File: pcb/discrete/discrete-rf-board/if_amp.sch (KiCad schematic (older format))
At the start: 48 parts, among them Q23 NSVT65011MW6T1G, Q24 Q_NPN_BCE, Q25 NSVT65011MW6T1G, U10 NLAS4157DFT2G, U11 NLAS4157DFT2G, U8 NLAS4157DFT2G, U9 NLAS4157DFT2G

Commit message: Autofill
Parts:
- TP1, TP10, TP2, TP3, TP4, TP5, TP6, TP8, TP9: footprint (none) -> TestPoint:TestPoint_Pad_D1.0mm; Mouser (none) -> NoPart
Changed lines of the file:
@@
 F 0 "TP9" H 7300 2370 50  0000 C CNN
 F 1 "TestPoint" H 7300 2300 50  0000 C CNN
-F 2 "" H 7500 2100 50  0001 C CNN
+F 2 "TestPoint:TestPoint_Pad_D1.0mm" H 7500 2100 50  0001 C CNN
 F 3 "~" H 7500 2100 50  0001 C CNN
+F 4 "NoPart" H 7500 2100 50  0001 C CNN "Mouser"
 	1    7300 2100
 	1    0    0    -1
@@
 F 0 "TP8" H 6550 3620 50  0000 C CNN
 F 1 "TestPoint" H 6550 3550 50  0000 C CNN
-F 2 "" H 6750 3350 50  0001 C CNN
+F 2 "TestPoint:TestPoint_Pad_D1.0mm" H 6750 3350 50  0001 C CNN
 F 3 "~" H 6750 3350 50  0001 C CNN
+F 4 "NoPart" H 6750 3350 50  0001 C CNN "Mouser"
 	1    6550 3350
 	1    0    0    -1
@@
 F 0 "TP2" H 2050 3570 50  0000 C CNN
 F 1 "TestPoint" H 2050 3500 50  0000 C CNN
-F 2 "" H 2250 3300 50  0001 C CNN
+F 2 "TestPoint:TestPoint_Pad_D1.0mm" H 2250 3300 50  0001 C CNN
 F 3 "~" H 2250 3300 50  0001 C CNN
+F 4 "NoPart" H 2250 3300 50  0001 C CNN "Mouser"
 	1    2050 3300
 	-1   0    0    1
@@
 F 0 "TP1" H 1650 2670 50  0000 C CNN
 F 1 "TestPoint" H 1650 2600 50  0000 C CNN
-F 2 "" H 1850 2400 50  0001 C CNN
+F 2 "TestPoint:TestPoint_Pad_D1.0mm" H 1850 2400 50  0001 C CNN
 F 3 "~" H 1850 2400 50  0001 C CNN
+F 4 "NoPart" H 1850 2400 50  0001 C CNN "Mouser"
 	1    1650 2400
 	1    0    0    -1
@@
 F 0 "TP5" H 3250 2620 50  0000 C CNN
 F 1 "TestPoint" H 3250 2550 50  0000 C CNN
-F 2 "" H 3450 2350 50  0001 C CNN
+F 2 "TestPoint:TestPoint_Pad_D1.0mm" H 3450 2350 50  0001 C CNN
 F 3 "~" H 3450 2350 50  0001 C CNN
+F 4 "NoPart" H 3450 2350 50  0001 C CNN "Mouser"
 	1    3250 2350
 	1    0    0    -1
@@
 F 0 "TP4" H 2350 4220 50  0000 C CNN
 F 1 "TestPoint" H 2350 4150 50  0000 C CNN
-F 2 "" H 2550 3950 50  0001 C CNN
+F 2 "TestPoint:TestPoint_Pad_D1.0mm" H 2550 3950 50  0001 C CNN
 F 3 "~" H 2550 3950 50  0001 C CNN
+F 4 "NoPart" H 2550 3950 50  0001 C CNN "Mouser"
 	1    2350 3950
 	0    -1   -1   0
@@
 F 0 "TP3" H 2100 1920 50  0000 C CNN
 F 1 "TestPoint" H 2100 1850 50  0000 C CNN
-F 2 "" H 2300 1650 50  0001 C CNN
+F 2 "TestPoint:TestPoint_Pad_D1.0mm" H 2300 1650 50  0001 C CNN
 F 3 "~" H 2300 1650 50  0001 C CNN
+F 4 "NoPart" H 2300 1650 50  0001 C CNN "Mouser"
 	1    2100 1650
 	1    0    0    -1
@@
 F 0 "TP6" H 5500 3170 50  0000 C CNN
 F 1 "TestPoint" H 5500 3100 50  0000 C CNN
-F 2 "" H 5700 2900 50  0001 C CNN
+F 2 "TestPoint:TestPoint_Pad_D1.0mm" H 5700 2900 50  0001 C CNN
 F 3 "~" H 5700 2900 50  0001 C CNN
+F 4 "NoPart" H 5700 2900 50  0001 C CNN "Mouser"
 	1    5500 2900
 	-1   0    0    1
@@
 F 0 "TP10" H 7750 3120 50  0000 C CNN
 F 1 "TestPoint" H 7750 3050 50  0000 C CNN
-F 2 "" H 7950 2850 50  0001 C CNN
+F 2 "TestPoint:TestPoint_Pad_D1.0mm" H 7950 2850 50  0001 C CNN
 F 3 "~" H 7950 2850 50  0001 C CNN
+F 4 "NoPart" H 7950 2850 50  0001 C CNN "Mouser"
 	1    7750 2850
 	-1   0    0    1

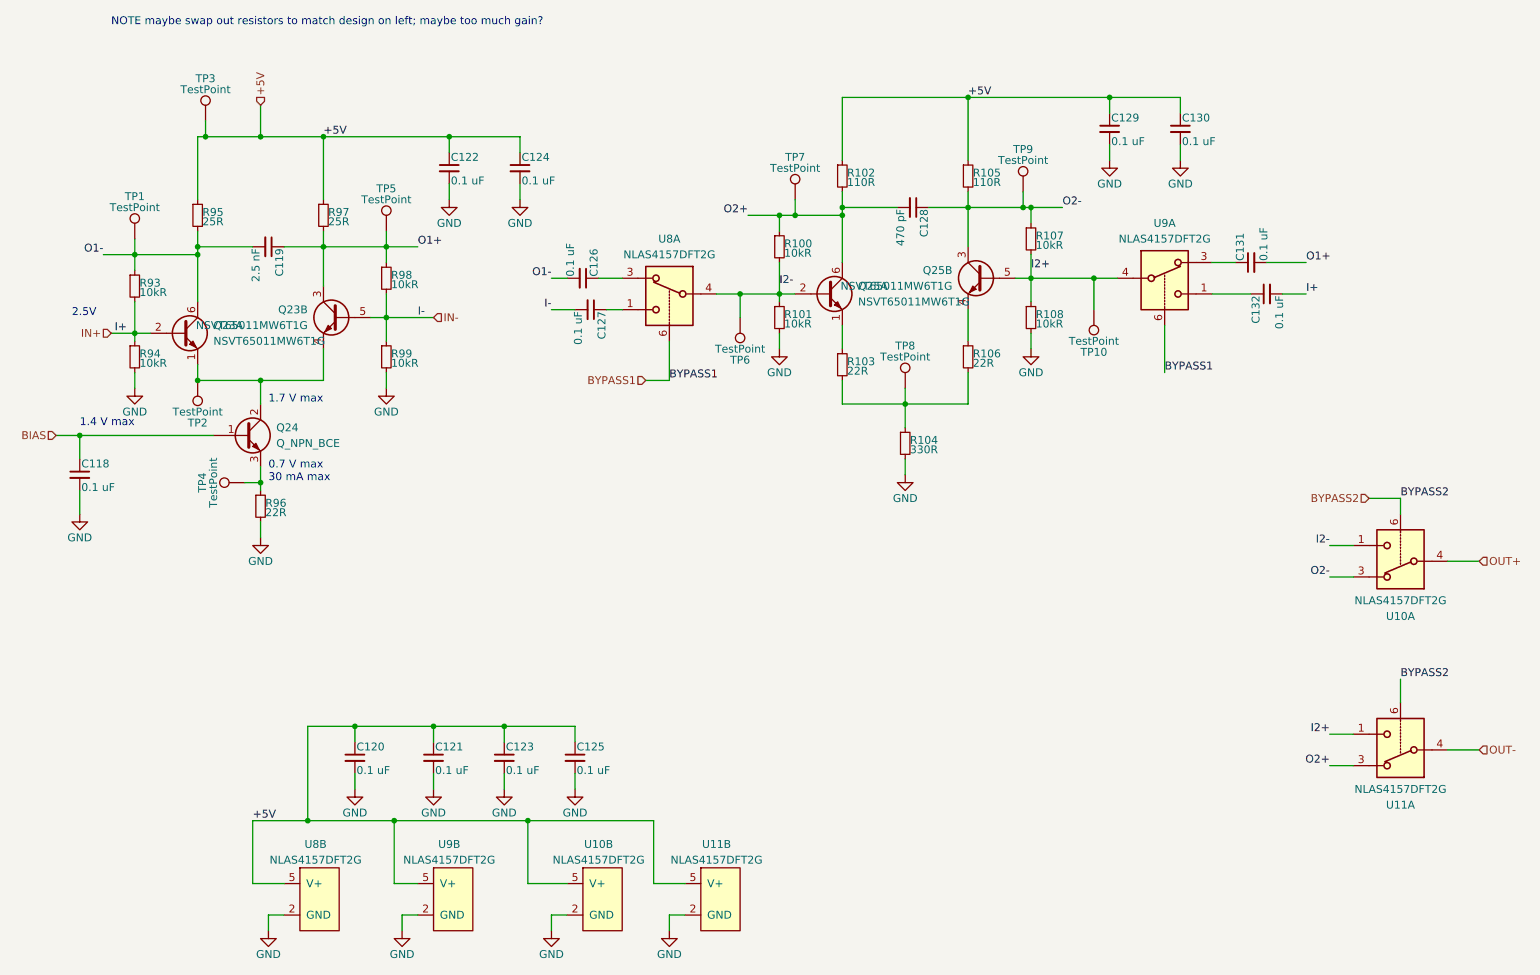
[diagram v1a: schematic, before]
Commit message: Add more footprints, saving before autofill
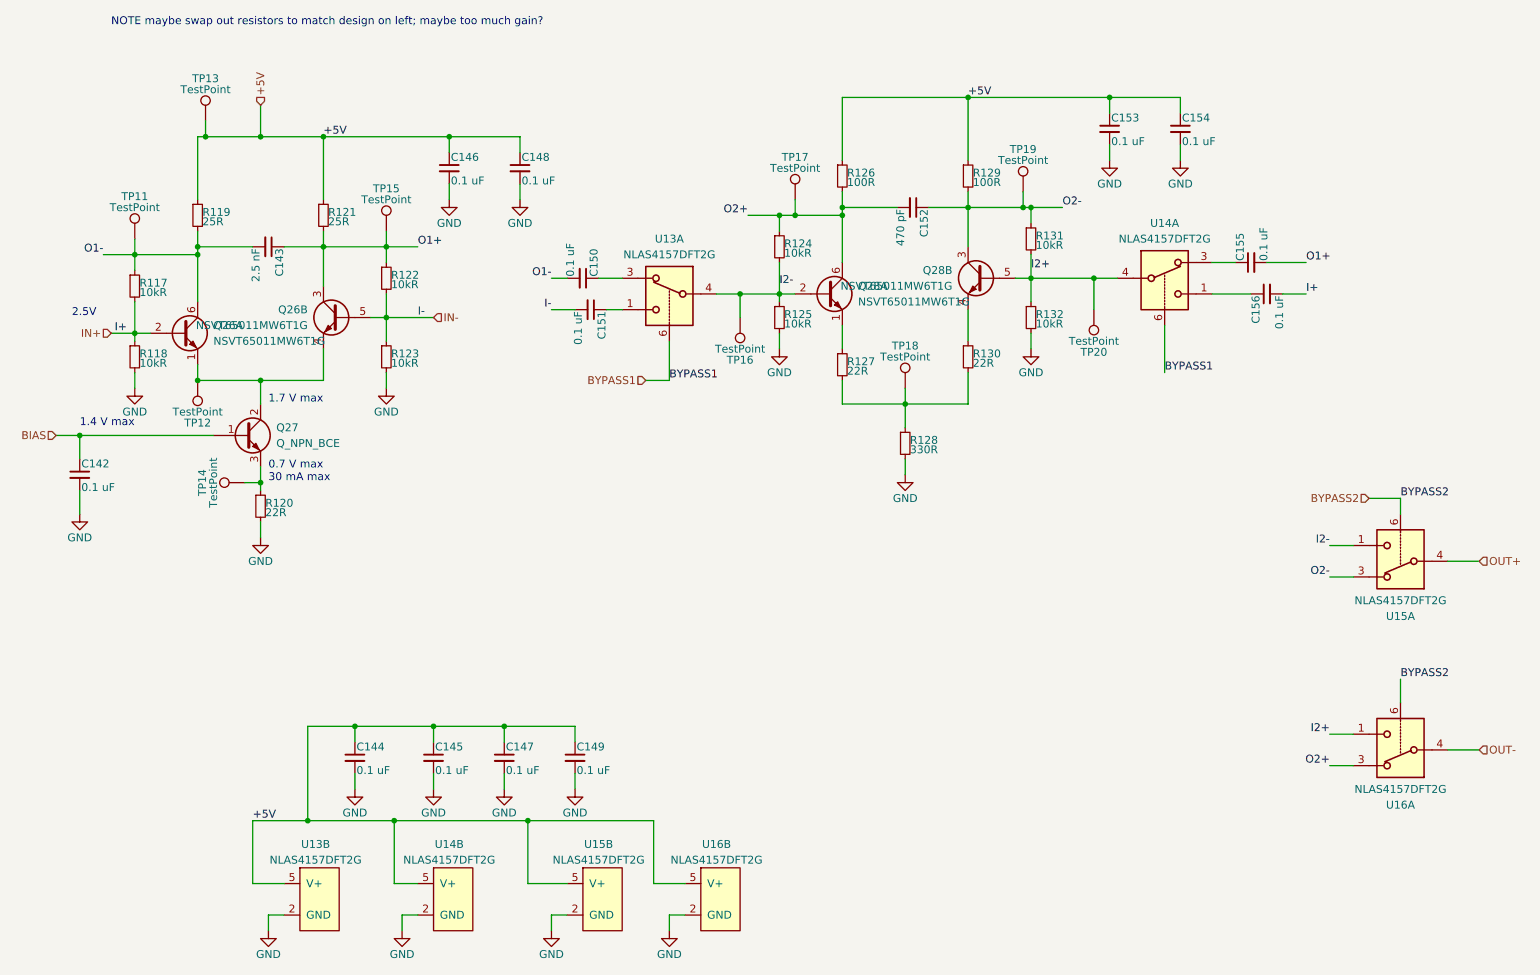
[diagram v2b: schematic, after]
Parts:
- R102, R105: value 110R -> 100R
- R99: footprint (none) -> Resistor_SMD:R_0402_1005Metric; Mouser (none) -> 603-AC0402FR-1310KL

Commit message: Autofill
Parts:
- C118, C120, C121, C122, C123, C124, C125, C126, C127, C129, C130, C131, C132: footprint (none) -> Capacitor_SMD:C_0402_1005Metric; Mouser (none) -> 80-C0402C104M4P
- R100, R101, R107, R108, R93, R94, R98: footprint (none) -> Resistor_SMD:R_0402_1005Metric; Mouser (none) -> 603-AC0402FR-1310KL
- R102, R105: footprint (none) -> Resistor_SMD:R_0402_1005Metric; Mouser (none) -> 667-ERJ-U02D1000X
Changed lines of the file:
@@
 F 0 "R117" H 1680 2720 50  0000 L CNN
 F 1 "10kR" H 1680 2660 50  0000 L CNN
-F 2 "" H 1650 2700 50  0001 C CNN
+F 2 "Resistor_SMD:R_0402_1005Metric" H 1650 2700 50  0001 C CNN
 F 3 "~" H 1650 2700 50  0001 C CNN
+F 4 "603-AC0402FR-1310KL" H 1650 2700 50  0001 C CNN "Mouser"
 	1    1650 2700
 	1    0    0    -1
@@
 F 0 "R118" H 1680 3170 50  0000 L CNN
 F 1 "10kR" H 1680 3110 50  0000 L CNN
-F 2 "" H 1650 3150 50  0001 C CNN
+F 2 "Resistor_SMD:R_0402_1005Metric" H 1650 3150 50  0001 C CNN
 F 3 "~" H 1650 3150 50  0001 C CNN
+F 4 "603-AC0402FR-1310KL" H 1650 3150 50  0001 C CNN "Mouser"
 	1    1650 3150
 	1    0    0    -1
@@
 F 0 "R122" H 3280 2670 50  0000 L CNN
 F 1 "10kR" H 3280 2610 50  0000 L CNN
-F 2 "" H 3250 2650 50  0001 C CNN
+F 2 "Resistor_SMD:R_0402_1005Metric" H 3250 2650 50  0001 C CNN
 F 3 "~" H 3250 2650 50  0001 C CNN
+F 4 "603-AC0402FR-1310KL" H 3250 2650 50  0001 C CNN "Mouser"
 	1    3250 2650
 	1    0    0    -1
@@
 F 0 "C142" H 1310 3970 50  0000 L CNN
 F 1 "0.1 uF" H 1310 3820 50  0000 L CNN
-F 2 "" H 1300 3900 50  0001 C CNN
+F 2 "Capacitor_SMD:C_0402_1005Metric" H 1300 3900 50  0001 C CNN
 F 3 "~" H 1300 3900 50  0001 C CNN
+F 4 "80-C0402C104M4P" H 1300 3900 50  0001 C CNN "Mouser"
 	1    1300 3900
 	1    0    0    -1
@@
 F 0 "R126" H 6180 2020 50  0000 L CNN
 F 1 "100R" H 6180 1960 50  0000 L CNN
-F 2 "" H 6150 2000 50  0001 C CNN
+F 2 "Resistor_SMD:R_0402_1005Metric" H 6150 2000 50  0001 C CNN
 F 3 "~" H 6150 2000 50  0001 C CNN
+F 4 " 667-ERJ-U02D1000X " H 6150 2000 50  0001 C CNN "Mouser"
 	1    6150 2000
 	1    0    0    -1
@@
 F 0 "R129" H 6980 2020 50  0000 L CNN
 F 1 "100R" H 6980 1960 50  0000 L CNN
-F 2 "" H 6950 2000 50  0001 C CNN
+F 2 "Resistor_SMD:R_0402_1005Metric" H 6950 2000 50  0001 C CNN
 F 3 "~" H 6950 2000 50  0001 C CNN
+F 4 " 667-ERJ-U02D1000X " H 6950 2000 50  0001 C CNN "Mouser"
 	1    6950 2000
 	1    0    0    -1
@@
 F 0 "R124" H 5780 2470 50  0000 L CNN
 F 1 "10kR" H 5780 2410 50  0000 L CNN
-F 2 "" H 5750 2450 50  0001 C CNN
+F 2 "Resistor_SMD:R_0402_1005Metric" H 5750 2450 50  0001 C CNN
 F 3 "~" H 5750 2450 50  0001 C CNN
+F 4 "603-AC0402FR-1310KL" H 5750 2450 50  0001 C CNN "Mouser"
 	1    5750 2450
 	1    0    0    -1
@@
 F 0 "R125" H 5780 2920 50  0000 L CNN
 F 1 "10kR" H 5780 2860 50  0000 L CNN
-F 2 "" H 5750 2900 50  0001 C CNN
+F 2 "Resistor_SMD:R_0402_1005Metric" H 5750 2900 50  0001 C CNN
 F 3 "~" H 5750 2900 50  0001 C CNN
+F 4 "603-AC0402FR-1310KL" H 5750 2900 50  0001 C CNN "Mouser"
 	1    5750 2900
 	1    0    0    -1
@@
 F 0 "R132" H 7380 2920 50  0000 L CNN
 F 1 "10kR" H 7380 2860 50  0000 L CNN
-F 2 "" H 7350 2900 50  0001 C CNN
+F 2 "Resistor_SMD:R_0402_1005Metric" H 7350 2900 50  0001 C CNN
 F 3 "~" H 7350 2900 50  0001 C CNN
+F 4 "603-AC0402FR-1310KL" H 7350 2900 50  0001 C CNN "Mouser"
 	1    7350 2900
 	1    0    0    -1
@@
 F 0 "R131" H 7380 2420 50  0000 L CNN
 F 1 "10kR" H 7380 2360 50  0000 L CNN
-F 2 "" H 7350 2400 50  0001 C CNN
+F 2 "Resistor_SMD:R_0402_1005Metric" H 7350 2400 50  0001 C CNN
 F 3 "~" H 7350 2400 50  0001 C CNN
+F 4 "603-AC0402FR-1310KL" H 7350 2400 50  0001 C CNN "Mouser"
 	1    7350 2400
 	1    0    0    -1
@@
 F 0 "C150" H 4510 2720 50  0000 L CNN
 F 1 "0.1 uF" H 4510 2570 50  0000 L CNN
-F 2 "" H 4500 2650 50  0001 C CNN
+F 2 "Capacitor_SMD:C_0402_1005Metric" H 4500 2650 50  0001 C CNN
 F 3 "~" H 4500 2650 50  0001 C CNN
+F 4 "80-C0402C104M4P" H 4500 2650 50  0001 C CNN "Mouser"
 	1    4500 2650
 	0    1    -1   0
@@
 F 0 "C155" H 8760 2620 50  0000 L CNN
 F 1 "0.1 uF" H 8760 2470 50  0000 L CNN
-F 2 "" H 8750 2550 50  0001 C CNN
+F 2 "Capacitor_SMD:C_0402_1005Metric" H 8750 2550 50  0001 C CNN
 F 3 "~" H 8750 2550 50  0001 C CNN
+F 4 "80-C0402C104M4P" H 8750 2550 50  0001 C CNN "Mouser"
 	1    8750 2550
 	0    -1   -1   0
@@
 F 0 "C151" H 4560 2920 50  0000 L CNN
 F 1 "0.1 uF" H 4560 2770 50  0000 L CNN
-F 2 "" H 4550 2850 50  0001 C CNN
+F 2 "Capacitor_SMD:C_0402_1005Metric" H 4550 2850 50  0001 C CNN
 F 3 "~" H 4550 2850 50  0001 C CNN
+F 4 "80-C0402C104M4P" H 4550 2850 50  0001 C CNN "Mouser"
 	1    4550 2850
 	0    1    1    0
@@
 F 0 "C156" H 8860 2820 50  0000 L CNN
 F 1 "0.1 uF" H 8860 2670 50  0000 L CNN
-F 2 "" H 8850 2750 50  0001 C CNN
+F 2 "Capacitor_SMD:C_0402_1005Metric" H 8850 2750 50  0001 C CNN
 F 3 "~" H 8850 2750 50  0001 C CNN
+F 4 "80-C0402C104M4P" H 8850 2750 50  0001 C CNN "Mouser"
 	1    8850 2750
 	0    -1   1    0
@@
 F 0 "C144" H 3060 5770 50  0000 L CNN
 F 1 "0.1 uF" H 3060 5620 50  0000 L CNN
-F 2 "" H 3050 5700 50  0001 C CNN
+F 2 "Capacitor_SMD:C_0402_1005Metric" H 3050 5700 50  0001 C CNN
 F 3 "~" H 3050 5700 50  0001 C CNN
+F 4 "80-C0402C104M4P" H 3050 5700 50  0001 C CNN "Mouser"
 	1    3050 5700
 	1    0    0    -1
@@
 F 0 "C145" H 3560 5770 50  0000 L CNN
 F 1 "0.1 uF" H 3560 5620 50  0000 L CNN
-F 2 "" H 3550 5700 50  0001 C CNN
+F 2 "Capacitor_SMD:C_0402_1005Metric" H 3550 5700 50  0001 C CNN
 F 3 "~" H 3550 5700 50  0001 C CNN
+F 4 "80-C0402C104M4P" H 3550 5700 50  0001 C CNN "Mouser"
 	1    3550 5700
 	1    0    0    -1
@@
 F 0 "C147" H 4010 5770 50  0000 L CNN
 F 1 "0.1 uF" H 4010 5620 50  0000 L CNN
-F 2 "" H 4000 5700 50  0001 C CNN
+F 2 "Capacitor_SMD:C_0402_1005Metric" H 4000 5700 50  0001 C CNN
 F 3 "~" H 4000 5700 50  0001 C CNN
+F 4 "80-C0402C104M4P" H 4000 5700 50  0001 C CNN "Mouser"
 	1    4000 5700
 	1    0    0    -1
@@
 F 0 "C149" H 4460 5770 50  0000 L CNN
 F 1 "0.1 uF" H 4460 5620 50  0000 L CNN
-F 2 "" H 4450 5700 50  0001 C CNN
+F 2 "Capacitor_SMD:C_0402_1005Metric" H 4450 5700 50  0001 C CNN
 F 3 "~" H 4450 5700 50  0001 C CNN
+F 4 "80-C0402C104M4P" H 4450 5700 50  0001 C CNN "Mouser"
 	1    4450 5700
 	1    0    0    -1
@@
 F 0 "C146" H 3660 2020 50  0000 L CNN
 F 1 "0.1 uF" H 3660 1870 50  0000 L CNN
-F 2 "" H 3650 1950 50  0001 C CNN
+F 2 "Capacitor_SMD:C_0402_1005Metric" H 3650 1950 50  0001 C CNN
 F 3 "~" H 3650 1950 50  0001 C CNN
+F 4 "80-C0402C104M4P" H 3650 1950 50  0001 C CNN "Mouser"
 	1    3650 1950
 	1    0    0    -1
@@
 F 0 "C148" H 4110 2020 50  0000 L CNN
 F 1 "0.1 uF" H 4110 1870 50  0000 L CNN
-F 2 "" H 4100 1950 50  0001 C CNN
+F 2 "Capacitor_SMD:C_0402_1005Metric" H 4100 1950 50  0001 C CNN
 F 3 "~" H 4100 1950 50  0001 C CNN
+F 4 "80-C0402C104M4P" H 4100 1950 50  0001 C CNN "Mouser"
 	1    4100 1950
 	1    0    0    -1
@@
 F 0 "C153" H 7860 1770 50  0000 L CNN
 F 1 "0.1 uF" H 7860 1620 50  0000 L CNN
-F 2 "" H 7850 1700 50  0001 C CNN
+F 2 "Capacitor_SMD:C_0402_1005Metric" H 7850 1700 50  0001 C CNN
 F 3 "~" H 7850 1700 50  0001 C CNN
+F 4 "80-C0402C104M4P" H 7850 1700 50  0001 C CNN "Mouser"
 	1    7850 1700
 	1    0    0    -1
@@
 F 0 "C154" H 8310 1770 50  0000 L CNN
 F 1 "0.1 uF" H 8310 1620 50  0000 L CNN
-F 2 "" H 8300 1700 50  0001 C CNN
+F 2 "Capacitor_SMD:C_0402_1005Metric" H 8300 1700 50  0001 C CNN
 F 3 "~" H 8300 1700 50  0001 C CNN
+F 4 "80-C0402C104M4P" H 8300 1700 50  0001 C CNN "Mouser"
 	1    8300 1700
 	1    0    0    -1

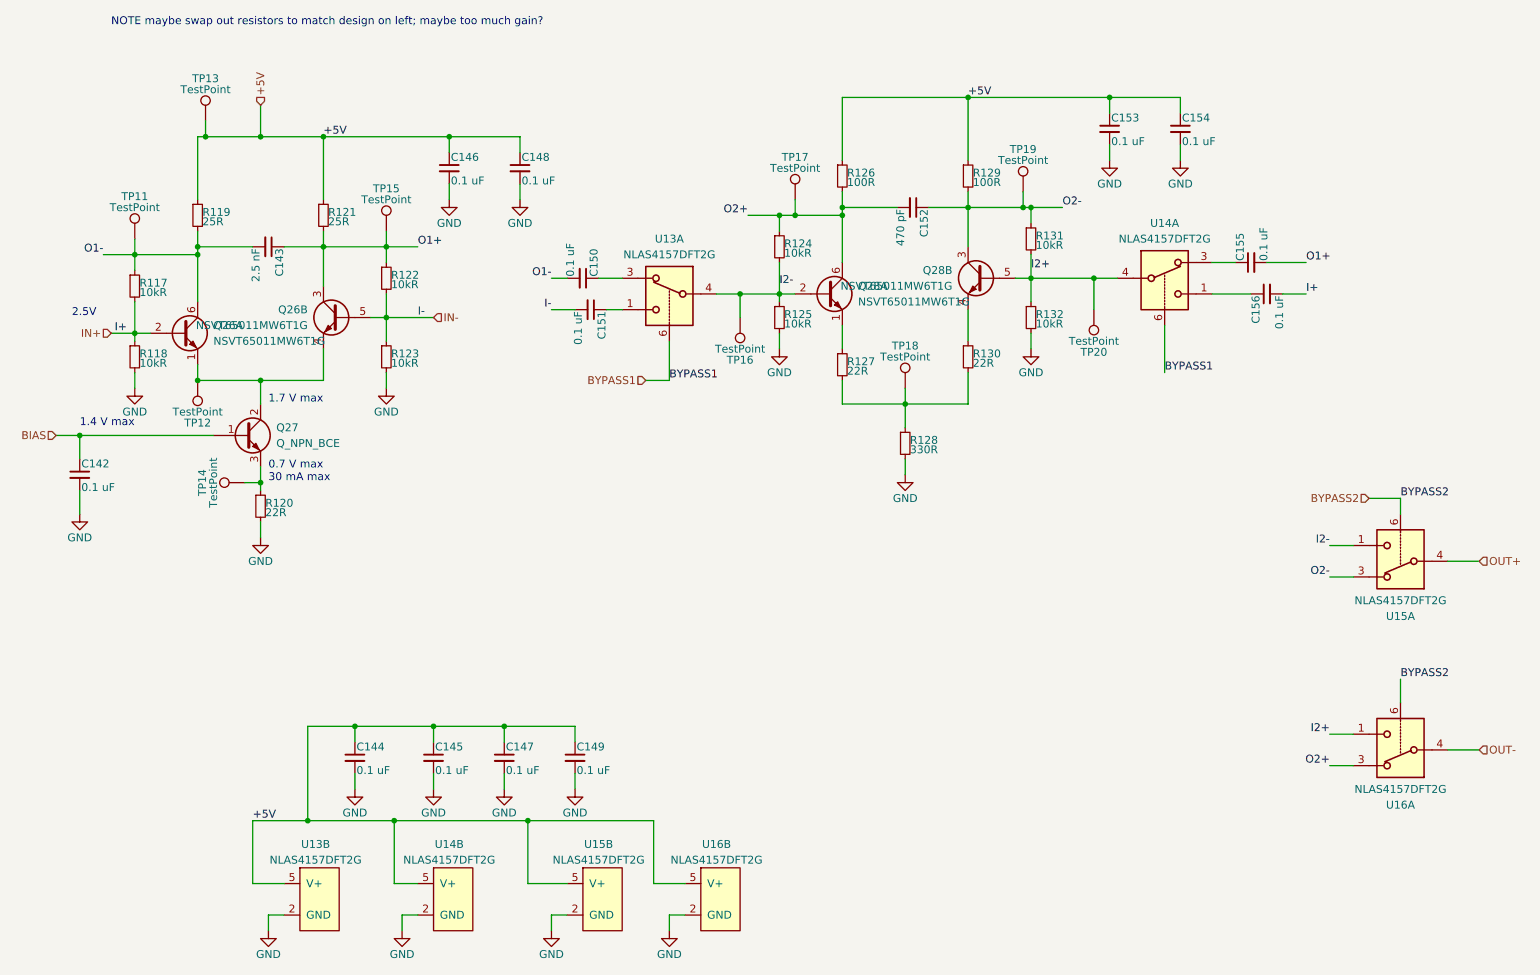
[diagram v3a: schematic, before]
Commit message: Reannotate everything; I'm trying to cut down the number of components
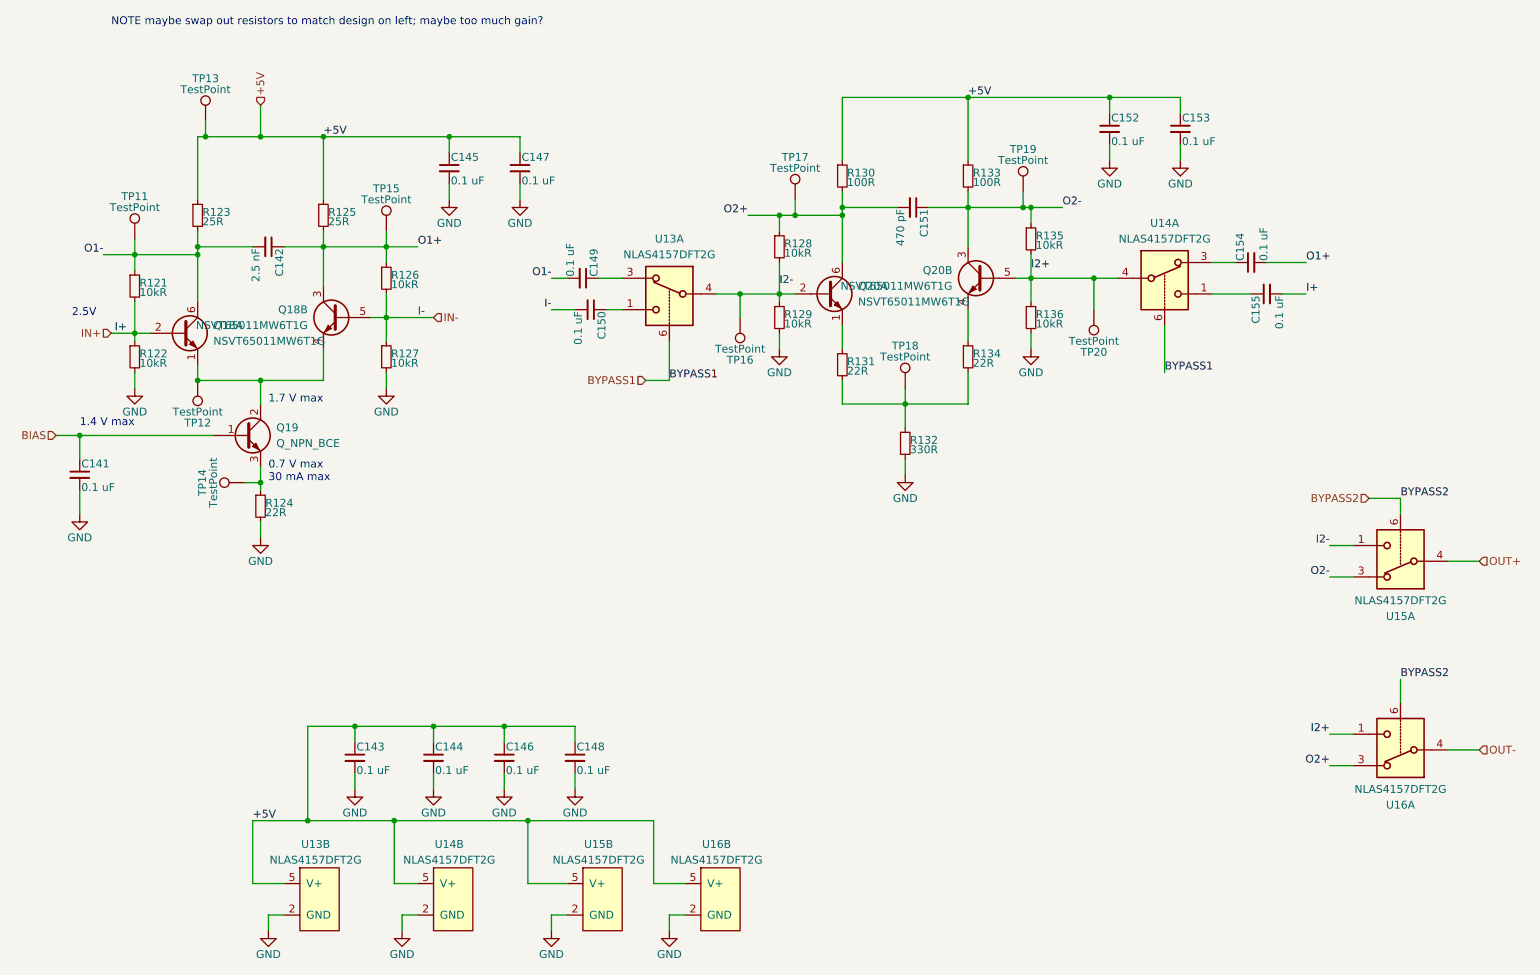
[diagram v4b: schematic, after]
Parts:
- renumbered C118 to C117, C119 to C118, C120 to C119, C121 to C120, C122 to C121, C123 to C122, C124 to C123, C125 to C124, C126 to C125, C127 to C126, C128 to C127, C129 to C128, C130 to C129, C131 to C130, C132 to C131, Q23 to Q15, Q24 to Q16, Q25 to Q17, R96 to R100, R97 to R101, R98 to R102, R99 to R103, R100 to R104, R101 to R105, R102 to R106, R103 to R107, R104 to R108, R105 to R109, R106 to R110, R107 to R111, R108 to R112, R93 to R97, R94 to R98, R95 to R99
